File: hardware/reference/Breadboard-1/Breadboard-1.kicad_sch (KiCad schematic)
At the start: 69 parts, among them J1 Left, J2 Right, J3 ICSP, J4 Oscilloscope, J5 TTL Serial, Q31 NCE2309, Q32 NCE2309, Q33 DMN6140L-7, Q34 DMN6140L-7, Q35 DTC143ZCA, Q36 DTC143ZCA, Q41 2N7002K, Q42 2N7002K, Q43 2N7002K, Q44 2N7002K, Q45 2N7002K, Q46 2N7002K, U11 ME6203A50M3G, U21 PIC18F16Q40-I/SS

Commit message: Updated BOM to optimize for JLCPCB production.
Used as many JLCPCB "basic" parts as possible, optimized for
the cheapest parts in stock as of today.
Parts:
- C11, C12: LCSC (none) -> C440198
- C21, C23, C31: LCSC (none) -> C49678
- C32: LCSC (none) -> C28323; Specification 0805 50V 100nF X7R 10% -> 0805 50V 1uF X7R 10%
- D11, D12, D13, D14: value B5819WS -> 1N5819; LCSC (none) -> C191023
- D41, D42, D51, D52, D53, D54, D55, D56: LCSC (none) -> C965818
- D57: LCSC (none) -> C965843
- FID1, FID2, FID3: Cost (none) -> 0; LCSC (none) -> DNP; Specification (none) -> DNP
- J1, J2, J3, J4, J5, JP61, U21: LCSC (none) -> DNP
- Q31, Q32: LCSC (none) -> C2843304
- Q33, Q34: value DMN6140L-7 -> DMN6140; LCSC (none) -> C211403
- Q35, Q36: LCSC (none) -> C15236
- Q41, Q42, Q43, Q44, Q45, Q46: value 2N7002K -> 2N7002; LCSC (none) -> C8545
- R21, R37, R51, R52, R53, R54, R55, R56, R57: LCSC (none) -> C17382
- R22, R35, R36: value 6K6 -> 6K65; LCSC (none) -> C17770
- R23, R31, R32: LCSC (none) -> C17414
- R24, R33, R34, R41, R42, R43, R44, R45, R46: LCSC (none) -> C17557
- R47, R48: LCSC (none) -> C17710
- R61: Cost 0.12 -> 0.03; LCSC (none) -> C876265
- U11: LCSC (none) -> C92717

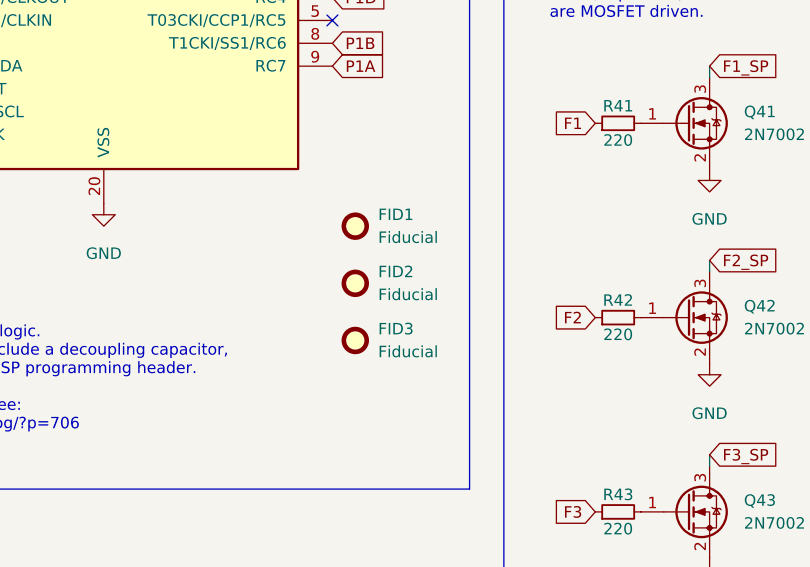
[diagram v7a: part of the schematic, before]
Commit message: Updates based on feedback from JLCPCB online tools.
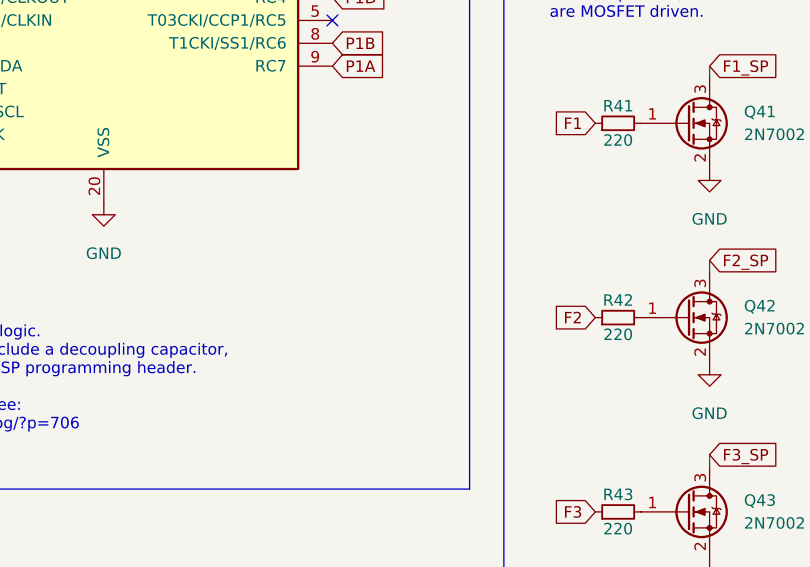
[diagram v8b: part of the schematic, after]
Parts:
- removed FID1, FID2, FID3: Fiducial, Fiducial:Fiducial_0.75mm_Mask2.25mm, symbol Mechanical:Fiducial
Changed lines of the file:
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@@
     (pin "3")
-  )
-  (symbol (lib_id "Mechanical:Fiducial") (at 101.6 132.08 0) (unit 1)
-    (in_bom yes) (on_board yes) (fields_autoplaced)
-    (property "Reference" "FID3" (id 0) (at 104.14 130.8099 0)
-      (effects (font (size 1.27 1.27)) (justify left))
-    )
-    (property "Value" "Fiducial" (id 1) (at 104.14 133.3499 0)
-      (effects (font (size 1.27 1.27)) (justify left))
-    )
-    (property "Footprint" "Fiducial:Fiducial_0.75mm_Mask2.25mm" (id 2) (at 101.6 132.08 0)
-      (effects (font (size 1.27 1.27)) hide)
-    )
-    (property "Datasheet" "" (id 3) (at 101.6 132.08 0)
-      (effects (font (size 1.27 1.27)) hide)
-    )
-    (property "Cost" "0" (id 4) (at 101.6 132.08 0)
-      (effects (font (size 1.27 1.27)) hide)
-    )
-    (property "LCSC" "DNP" (id 5) (at 101.6 132.08 0)
-      (effects (font (size 1.27 1.27)) hide)
-    )
-    (property "Specification" "DNP" (id 6) (at 101.6 132.08 0)
-      (effects (font (size 1.27 1.27)) hide)
-    )
   )
   (symbol (lib_id "power:Vdrive") (at 198.12 104.775 0) (unit 1)
@@
     (pin "2")
   )
-  (symbol (lib_id "Mechanical:Fiducial") (at 101.6 125.73 0) (unit 1)
-    (in_bom yes) (on_board yes) (fields_autoplaced)
-    (property "Reference" "FID2" (id 0) (at 104.14 124.4599 0)
-      (effects (font (size 1.27 1.27)) (justify left))
-    )
-    (property "Value" "Fiducial" (id 1) (at 104.14 126.9999 0)
-      (effects (font (size 1.27 1.27)) (justify left))
-    )
-    (property "Footprint" "Fiducial:Fiducial_0.75mm_Mask2.25mm" (id 2) (at 101.6 125.73 0)
-      (effects (font (size 1.27 1.27)) hide)
-    )
-    (property "Datasheet" "" (id 3) (at 101.6 125.73 0)
-      (effects (font (size 1.27 1.27)) hide)
-    )
-    (property "Cost" "0" (id 4) (at 101.6 125.73 0)
-      (effects (font (size 1.27 1.27)) hide)
-    )
-    (property "LCSC" "DNP" (id 5) (at 101.6 125.73 0)
-      (effects (font (size 1.27 1.27)) hide)
-    )
-    (property "Specification" "DNP" (id 6) (at 101.6 125.73 0)
-      (effects (font (size 1.27 1.27)) hide)
-    )
-  )
   (symbol (lib_id "power:GND") (at 170.18 29.21 0) (unit 1)
     (in_bom yes) (on_board yes)
@@
     (pin "2")
     (pin "3")
-  )
-  (symbol (lib_id "Mechanical:Fiducial") (at 101.6 119.38 0) (unit 1)
-    (in_bom yes) (on_board yes) (fields_autoplaced)
-    (property "Reference" "FID1" (id 0) (at 104.14 118.1099 0)
-      (effects (font (size 1.27 1.27)) (justify left))
-    )
-    (property "Value" "Fiducial" (id 1) (at 104.14 120.6499 0)
-      (effects (font (size 1.27 1.27)) (justify left))
-    )
-    (property "Footprint" "Fiducial:Fiducial_0.75mm_Mask2.25mm" (id 2) (at 101.6 119.38 0)
-      (effects (font (size 1.27 1.27)) hide)
-    )
-    (property "Datasheet" "" (id 3) (at 101.6 119.38 0)
-      (effects (font (size 1.27 1.27)) hide)
-    )
-    (property "Cost" "0" (id 4) (at 101.6 119.38 0)
-      (effects (font (size 1.27 1.27)) hide)
-    )
-    (property "LCSC" "DNP" (id 5) (at 101.6 119.38 0)
-      (effects (font (size 1.27 1.27)) hide)
-    )
-    (property "Specification" "DNP" (id 6) (at 101.6 119.38 0)
-      (effects (font (size 1.27 1.27)) hide)
-    )
   )
   (symbol (lib_id "power:+5V") (at 100.33 25.4 0) (unit 1)
@@
       (reference "D57") (unit 1) (value "MOTOR DIR") (footprint "LED_SMD:LED_RGB_1210")
     )
-    (path "/b1e3d7d1-5e1a-4783-b95d-60ad9975723b"
-      (reference "FID1") (unit 1) (value "Fiducial") (footprint "Fiducial:Fiducial_0.75mm_Mask2.25mm")
-    )
-    (path "/89d0e1b6-392a-4bac-b2c2-159e11a37d08"
-      (reference "FID2") (unit 1) (value "Fiducial") (footprint "Fiducial:Fiducial_0.75mm_Mask2.25mm")
-    )
-    (path "/1559fcdf-2609-4899-b549-fce5da783422"
-      (reference "FID3") (unit 1) (value "Fiducial") (footprint "Fiducial:Fiducial_0.75mm_Mask2.25mm")
-    )
     (path "/84e5506c-143e-495f-9aa4-d3a71622f213"
